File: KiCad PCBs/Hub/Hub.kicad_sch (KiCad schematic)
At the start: 1 part, among them J1 Conn_02x04_Top_Bottom

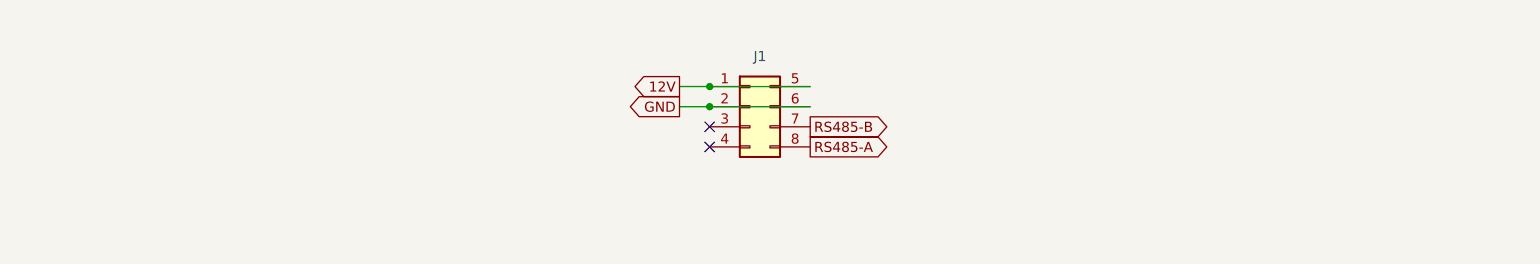
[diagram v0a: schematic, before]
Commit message: Added power status LEDs to Master PCB
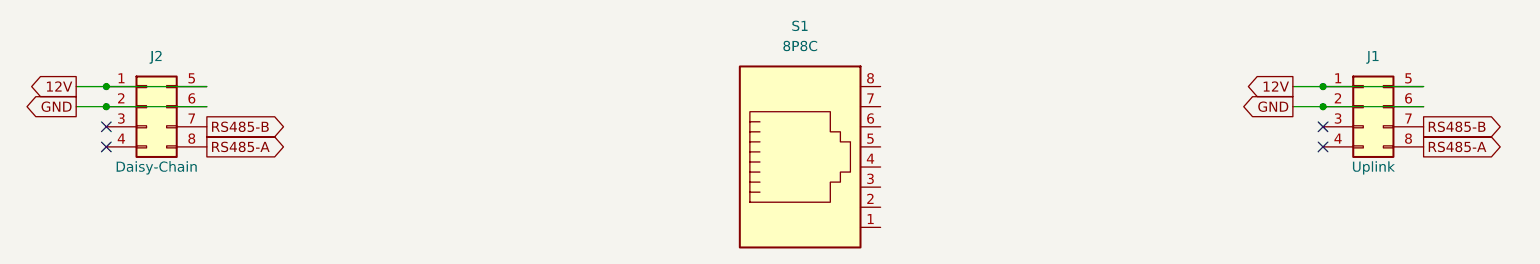
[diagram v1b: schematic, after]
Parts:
- added J2: Conn_02x04_Top_Bottom, A10 KiCad Libraries:Molex 43045-0800, symbol Connector_Generic:Conn_02x04_Top_Bottom
- added S1: 8P8C, A10 KiCad Libraries:RJ45-8P8C, symbol Connector:8P8C
- J1: Field4 (none) -> Uplink
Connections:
- net 12V: now also J2.1 (Pin_1), J2.5 (Pin_5)
- net GND: now also J2.2 (Pin_2), J2.6 (Pin_6)
- net RS485-A: now also J2.8 (Pin_8)
- net RS485-B: now also J2.7 (Pin_7)
- no-connect marks 2 -> 4
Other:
- moved on the sheet: J1
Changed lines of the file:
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@@
 (kicad_sch (version 20211123) (generator eeschema)
   (paper "A4")
-  (junction (at 138.43 104.14) (diameter 0) (color 0 0 0 0)
+  (junction (at 215.9 104.14) (diameter 0) (color 0 0 0 0)
   )
-  (junction (at 138.43 106.68) (diameter 0) (color 0 0 0 0)
+  (junction (at 62.23 104.14) (diameter 0) (color 0 0 0 0)
   )
-  (no_connect (at 138.43 109.22))
-  (no_connect (at 138.43 111.76))
-  (wire (pts (xy 138.43 104.14) (xy 151.13 104.14))
+  (junction (at 215.9 106.68) (diameter 0) (color 0 0 0 0)
+  )
+  (junction (at 62.23 106.68) (diameter 0) (color 0 0 0 0)
+  )
+  (no_connect (at 62.23 109.22))
+  (no_connect (at 215.9 109.22))
+  (no_connect (at 62.23 111.76))
+  (no_connect (at 215.9 111.76))
+  (wire (pts (xy 215.9 104.14) (xy 228.6 104.14))
     (stroke (width 0) (type default) (color 0 0 0 0))
   )
-  (wire (pts (xy 134.62 104.14) (xy 138.43 104.14))
+  (wire (pts (xy 212.09 104.14) (xy 215.9 104.14))
     (stroke (width 0) (type default) (color 0 0 0 0))
   )
-  (wire (pts (xy 138.43 106.68) (xy 151.13 106.68))
+  (wire (pts (xy 58.42 104.14) (xy 62.23 104.14))
     (stroke (width 0) (type default) (color 0 0 0 0))
   )
-  (wire (pts (xy 134.62 106.68) (xy 138.43 106.68))
+  (wire (pts (xy 62.23 106.68) (xy 74.93 106.68))
     (stroke (width 0) (type default) (color 0 0 0 0))
   )
-  (global_label "RS485-A" (shape output) (at 151.13 111.76 0) (fields_autoplaced)
+  (wire (pts (xy 215.9 106.68) (xy 228.6 106.68))
+    (stroke (width 0) (type default) (color 0 0 0 0))
+  )
+  (wire (pts (xy 62.23 104.14) (xy 74.93 104.14))
+    (stroke (width 0) (type default) (color 0 0 0 0))
+  )
+  (wire (pts (xy 58.42 106.68) (xy 62.23 106.68))
+    (stroke (width 0) (type default) (color 0 0 0 0))
+  )
+  (wire (pts (xy 212.09 106.68) (xy 215.9 106.68))
+    (stroke (width 0) (type default) (color 0 0 0 0))
+  )
+  (global_label "RS485-A" (shape output) (at 228.6 111.76 0) (fields_autoplaced)
     (effects (font (size 1.27 1.27)) (justify left))
-    (property "Intersheet References" "${INTERSHEET_REFS}" (id 0) (at 162.3121 111.6806 0)
+    (property "Intersheet References" "${INTERSHEET_REFS}" (id 0) (at 239.7821 111.6806 0)
       (effects (font (size 1.27 1.27)) (justify left) hide)
     )
   )
-  (global_label "12V" (shape output) (at 134.62 104.14 180) (fields_autoplaced)
+  (global_label "GND" (shape output) (at 58.42 106.68 180) (fields_autoplaced)
     (effects (font (size 1.27 1.27)) (justify right))
-    (property "Intersheet References" "${INTERSHEET_REFS}" (id 0) (at 128.6993 104.0606 0)
+    (property "Intersheet References" "${INTERSHEET_REFS}" (id 0) (at 52.1364 106.6006 0)
       (effects (font (size 1.27 1.27)) (justify right) hide)
     )
   )
-  (global_label "RS485-B" (shape output) (at 151.13 109.22 0) (fields_autoplaced)
+  (global_label "12V" (shape output) (at 58.42 104.14 180) (fields_autoplaced)
+    (effects (font (size 1.27 1.27)) (justify right))
+    (property "Intersheet References" "${INTERSHEET_REFS}" (id 0) (at 52.4993 104.0606 0)
+      (effects (font (size 1.27 1.27)) (justify right) hide)
+    )
+  )
+  (global_label "RS485-B" (shape output) (at 74.93 109.22 0) (fields_autoplaced)
     (effects (font (size 1.27 1.27)) (justify left))
-    (property "Intersheet References" "${INTERSHEET_REFS}" (id 0) (at 162.4936 109.1406 0)
+    (property "Intersheet References" "${INTERSHEET_REFS}" (id 0) (at 86.2936 109.1406 0)
       (effects (font (size 1.27 1.27)) (justify left) hide)
     )
   )
-  (global_label "GND" (shape output) (at 134.62 106.68 180) (fields_autoplaced)
+  (global_label "12V" (shape output) (at 212.09 104.14 180) (fields_autoplaced)
     (effects (font (size 1.27 1.27)) (justify right))
-    (property "Intersheet References" "${INTERSHEET_REFS}" (id 0) (at 128.3364 106.6006 0)
+    (property "Intersheet References" "${INTERSHEET_REFS}" (id 0) (at 206.1693 104.0606 0)
       (effects (font (size 1.27 1.27)) (justify right) hide)
     )
   )
-  (symbol (lib_id "Connector_Generic:Conn_02x04_Top_Bottom") (at 143.51 106.68 0) (unit 1)
+  (global_label "RS485-A" (shape output) (at 74.93 111.76 0) (fields_autoplaced)
+    (effects (font (size 1.27 1.27)) (justify left))
+    (property "Intersheet References" "${INTERSHEET_REFS}" (id 0) (at 86.1121 111.6806 0)
+      (effects (font (size 1.27 1.27)) (justify left) hide)
+    )
+  )
+  (global_label "RS485-B" (shape output) (at 228.6 109.22 0) (fields_autoplaced)
+    (effects (font (size 1.27 1.27)) (justify left))
+    (property "Intersheet References" "${INTERSHEET_REFS}" (id 0) (at 239.9636 109.1406 0)
+      (effects (font (size 1.27 1.27)) (justify left) hide)
+    )
+  )
+  (global_label "GND" (shape output) (at 212.09 106.68 180) (fields_autoplaced)
+    (effects (font (size 1.27 1.27)) (justify right))
+    (property "Intersheet References" "${INTERSHEET_REFS}" (id 0) (at 205.8064 106.6006 0)
+      (effects (font (size 1.27 1.27)) (justify right) hide)
+    )
+  )
+  (symbol (lib_id "Connector_Generic:Conn_02x04_Top_Bottom") (at 220.98 106.68 0) (unit 1)
     (in_bom yes) (on_board yes)
-    (property "Reference" "J1" (id 0) (at 144.78 100.33 0))
-    (property "Value" "Conn_02x04_Top_Bottom" (id 1) (at 144.78 100.33 0)
+    (property "Reference" "J1" (id 0) (at 222.25 100.33 0))
+    (property "Value" "Conn_02x04_Top_Bottom" (id 1) (at 222.25 100.33 0)
       (effects (font (size 1.27 1.27)) hide)
     )
-    (property "Footprint" "A10 KiCad Libraries:Molex 43045-0800" (id 2) (at 143.51 106.68 0)
+    (property "Footprint" "A10 KiCad Libraries:Molex 43045-0800" (id 2) (at 220.98 106.68 0)
       (effects (font (size 1.27 1.27)) hide)
     )
-    (property "Datasheet" "~" (id 3) (at 143.51 106.68 0)
+    (property "Datasheet" "~" (id 3) (at 220.98 106.68 0)
       (effects (font (size 1.27 1.27)) hide)
     )
+    (property "Field4" "Uplink" (id 4) (at 222.25 114.3 0))
+    (pin "1")
+    (pin "2")
+    (pin "3")
+    (pin "4")
+    (pin "5")
+    (pin "6")
+    (pin "7")
+    (pin "8")
+  )
+  (symbol (lib_id "Connector:8P8C") (at 149.86 114.3 0) (unit 1)
+    (in_bom yes) (on_board yes) (fields_autoplaced)
+    (property "Reference" "S1" (id 0) (at 149.86 96.52 0))
+    (property "Value" "8P8C" (id 1) (at 149.86 99.06 0))
+    (property "Footprint" "A10 KiCad Libraries:RJ45-8P8C" (id 2) (at 149.86 113.665 90)
+      (effects (font (size 1.27 1.27)) hide)
+    )
+    (property "Datasheet" "~" (id 3) (at 149.86 113.665 90)
+      (effects (font (size 1.27 1.27)) hide)
+    )
+    (pin "1")
+    (pin "2")
+    (pin "3")
+    (pin "4")
+    (pin "5")
+    (pin "6")
+    (pin "7")
+    (pin "8")
+  )
+  (symbol (lib_id "Connector_Generic:Conn_02x04_Top_Bottom") (at 67.31 106.68 0) (unit 1)
+    (in_bom yes) (on_board yes)
+    (property "Reference" "J2" (id 0) (at 68.58 100.33 0))
+    (property "Value" "Conn_02x04_Top_Bottom" (id 1) (at 68.58 100.33 0)
+      (effects (font (size 1.27 1.27)) hide)
+    )
+    (property "Footprint" "A10 KiCad Libraries:Molex 43045-0800" (id 2) (at 67.31 106.68 0)
+      (effects (font (size 1.27 1.27)) hide)
+    )
+    (property "Datasheet" "~" (id 3) (at 67.31 106.68 0)
+      (effects (font (size 1.27 1.27)) hide)
+    )
+    (property "Field4" "Daisy-Chain" (id 4) (at 68.58 114.3 0))
     (pin "1")
     (pin "2")
@@
       (reference "J1") (unit 1) (value "Conn_02x04_Top_Bottom") (footprint "A10 KiCad Libraries:Molex 43045-0800")
     )
+    (path "/f3838ace-e55c-44ba-83f3-9fab14bb9d00"
+      (reference "J2") (unit 1) (value "Conn_02x04_Top_Bottom") (footprint "A10 KiCad Libraries:Molex 43045-0800")
+    )
+    (path "/326a8d94-eb30-43b8-8aed-9cea4f3abf49"
+      (reference "S1") (unit 1) (value "8P8C") (footprint "A10 KiCad Libraries:RJ45-8P8C")
+    )
   )

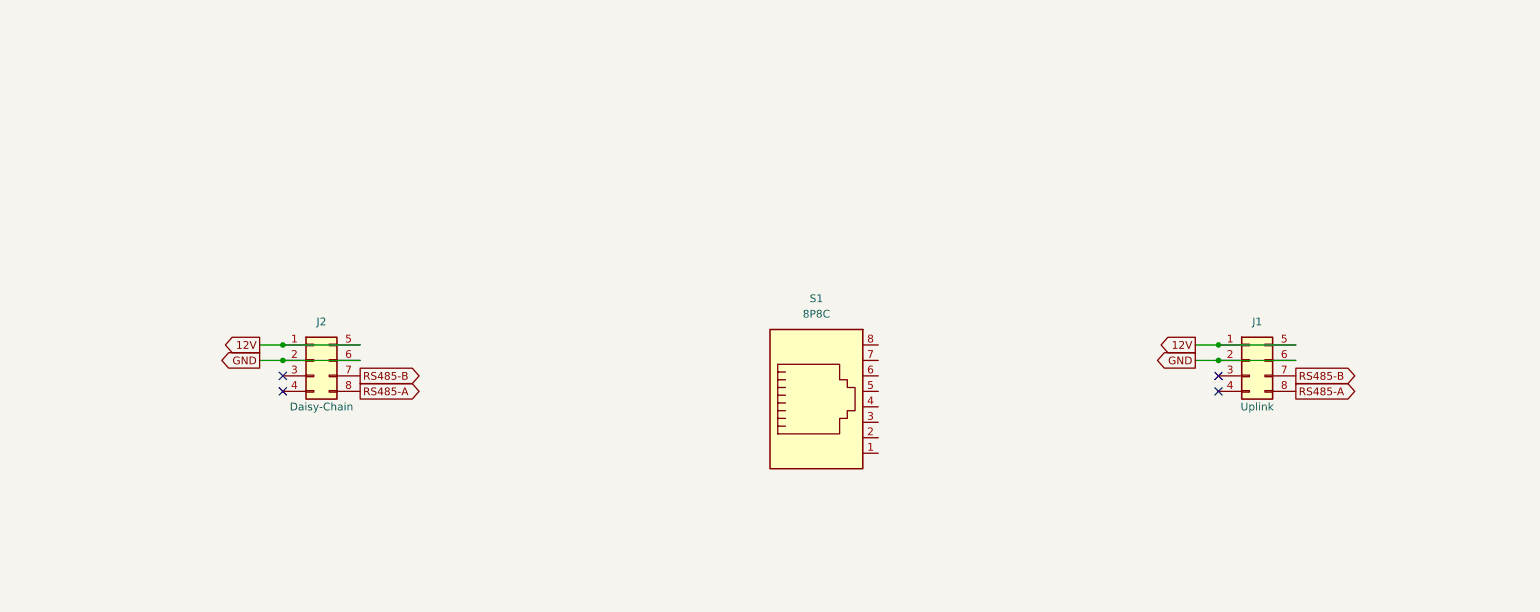
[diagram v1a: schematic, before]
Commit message: Updated Master PCB and completed first version of Hub
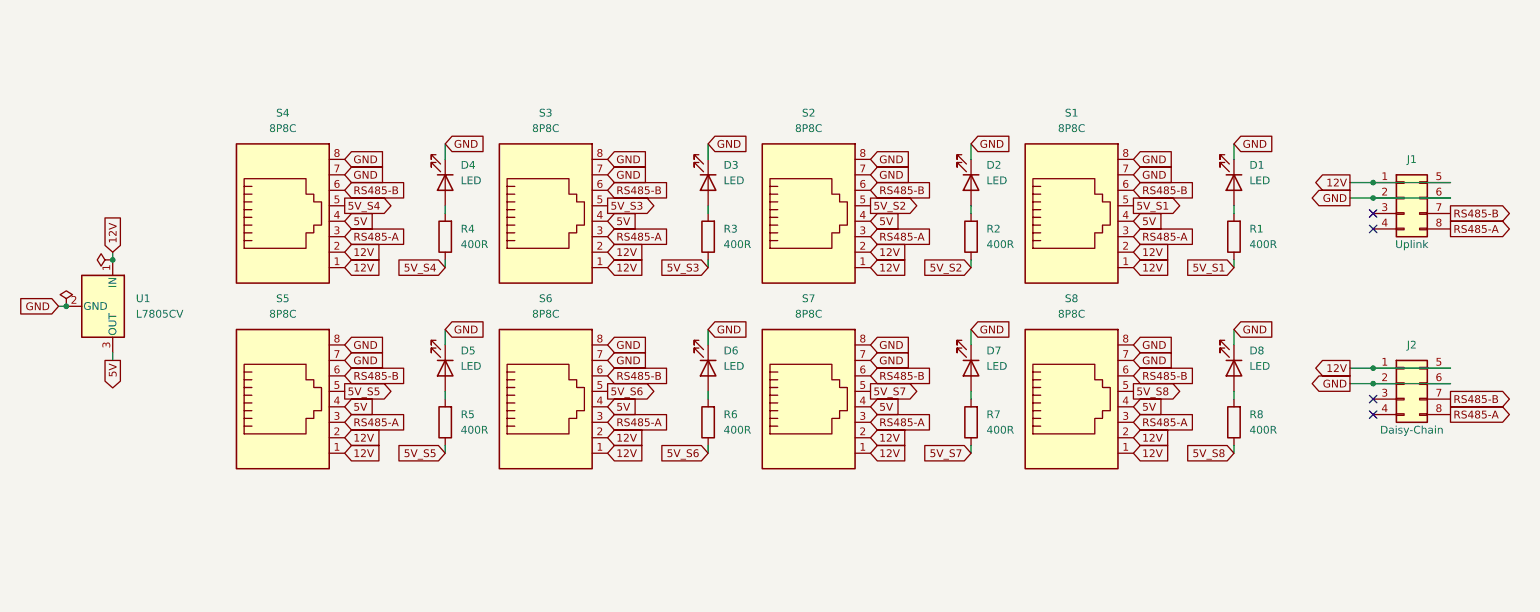
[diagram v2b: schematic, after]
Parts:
- added D1, D2, D3, D4, D5, D6, D7, D8: LED, LED_SMD:LED_1210_3225Metric_Pad1.42x2.65mm_HandSolder, symbol Device:LED
- added R1, R2, R3, R4, R5, R6, R7, R8: 400R, Resistor_SMD:R_1210_3225Metric_Pad1.30x2.65mm_HandSolder, symbol Device:R
- added S2, S3, S4, S5, S6, S7, S8: 8P8C, A10 KiCad Libraries:RJ45-8P8C, symbol Connector:8P8C
- added U1: L7805CV, Package_TO_SOT_THT:TO-220-3_Vertical, symbol Regulator_Linear:L7805
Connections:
- net 12V: now also S1.1, S1.2, S2.1, S2.2, S3.1, S3.2, S4.1, S4.2, S5.1, S5.2, S6.1, S6.2, S7.1, S7.2, S8.1, S8.2, U1.1 (IN)
- net GND: now also S1.7, S1.8, D1.1 (K), D2.1 (K), D3.1 (K), D4.1 (K), D5.1 (K), D6.1 (K), D7.1 (K), D8.1 (K), S2.7, S2.8, S3.7, S3.8, S4.7, S4.8, S5.7, S5.8, S6.7, S6.8, S7.7, S7.8, S8.7, S8.8, U1.2 (GND)
- net RS485-A: now also S1.3, S2.3, S3.3, S4.3, S5.3, S6.3, S7.3, S8.3
- net RS485-B: now also S1.6, S2.6, S3.6, S4.6, S5.6, S6.6, S7.6, S8.6
- net 5V: now reaches S1.4
- net 5V: now also S2.4, S3.4, S4.4, S5.4, S6.4, S7.4, S8.4, U1.3 (OUT)
- net 5V_S1: now reaches S1.5
- net 5V_S1: now also R1.1
- new net: D6.2 (A), R6.2
- new net: D5.2 (A), R5.2
- new net: D2.2 (A), R2.2
- new net: D4.2 (A), R4.2
- new net: D7.2 (A), R7.2
- new net: D8.2 (A), R8.2
- new net: D1.2 (A), R1.2
- new net: D3.2 (A), R3.2
- new net 5V_S2: R2.1, S2.5
- new net 5V_S3: R3.1, S3.5
- new net 5V_S4: R4.1, S4.5
- new net 5V_S5: R5.1, S5.5
- new net 5V_S6: R6.1, S6.5
- new net 5V_S7: R7.1, S7.5
- new net 5V_S8: R8.1, S8.5
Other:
- moved on the sheet: J1, J2, S1

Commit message: First version of Hub completed
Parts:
- removed D1, D2, D3, D4, D5, D6, D7, D8: LED, LED_SMD:LED_1210_3225Metric_Pad1.42x2.65mm_HandSolder, symbol Device:LED
- removed S1, S2, S3, S4, S5, S6, S7, S8: 8P8C, A10 KiCad Libraries:RJ45-8P8C, symbol Connector:8P8C
- removed U1: L7805CV, Package_TO_SOT_THT:TO-220-3_Vertical, symbol Regulator_Linear:L7805
- added R10, R12, R14, R16: 1.8K, A10 KiCad Libraries:R0805, symbol Device:R
- added R11, R13, R15, R9: 390R, A10 KiCad Libraries:R0805, symbol Device:R
- added U2, U3: RJ45-B-1*4, A10 KiCad Libraries:RJ45-TH_B-1-4, symbol A10:RJ45-B-1*4
- J1, J2: footprint A10 KiCad Libraries:Molex 43045-0800 -> A10 KiCad Libraries:Molex Micro-Fit 3.0 43045-0800
- R1, R3, R5, R7: value 400R -> 390R; footprint Resistor_SMD:R_1210_3225Metric_Pad1.30x2.65mm_HandSolder -> A10 KiCad Libraries:R0805
- R2, R4, R6, R8: value 400R -> 1.8K; footprint Resistor_SMD:R_1210_3225Metric_Pad1.30x2.65mm_HandSolder -> A10 KiCad Libraries:R0805
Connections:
- net 12V: now also U2.12, U2.16, U2.17, U2.24, U2.28, U2.29, U2.36, U2.4, U2.40, U2.41, U2.48, U2.5, U3.12, U3.16, U3.17, U3.24, U3.28, U3.29, U3.36, U3.4, U3.40, U3.41, U3.48, U3.5
- net 5V_S1: now also U2.1, U2.10; no longer R1.1
- net 5V_S2: now also U2.13, U2.22; no longer R2.1
- net 5V_S3: now also U2.25, U2.34; no longer R3.1
- net 5V_S4: now also U2.37, U2.46; no longer R4.1
- net 5V_S5: now also U3.1, U3.10; no longer R5.1
- net 5V_S6: now also U3.13, U3.22; no longer R6.1
- net 5V_S7: now also U3.25, U3.34; no longer R7.1
- net 5V_S8: now also U3.37, U3.46; no longer R8.1
- net GND: now also R1.1, R2.1, R3.1, R4.1, R5.1, R6.1, R7.1, R8.1, R10.1, R11.1, R12.1, R13.1, R14.1, R15.1, R16.1, R9.1, U2.0, U2.19, U2.20, U2.31, U2.32, U2.43, U2.44, U2.7, U2.8, U3.0, U3.19, U3.20, U3.31, U3.32, U3.43, U3.44, U3.7, U3.8
- net at R6.2: now also U2.23
- net at R5.2: now also U2.21
- net at R2.2: now also U2.11
- net at R4.2: now also U3.11
- net at R7.2: now also U3.21
- net at R8.2: now also U3.23
- net at R1.2: now also U2.9
- net at R3.2: now also U3.9
- net RS485-A renamed RS485+
- net RS485+: now also U2.15, U2.27, U2.3, U2.39, U3.15, U3.27, U3.3, U3.39
- net RS485-B renamed RS485-
- net RS485-: now also U2.18, U2.30, U2.42, U2.6, U3.18, U3.30, U3.42, U3.6
- new net: R14.2, U2.47
- new net: R13.2, U2.45
- new net: R15.2, U3.45
- new net: R9.2, U2.33
- new net: R10.2, U2.35
- new net: R11.2, U3.33
- new net: R12.2, U3.35
- new net: R16.2, U3.47

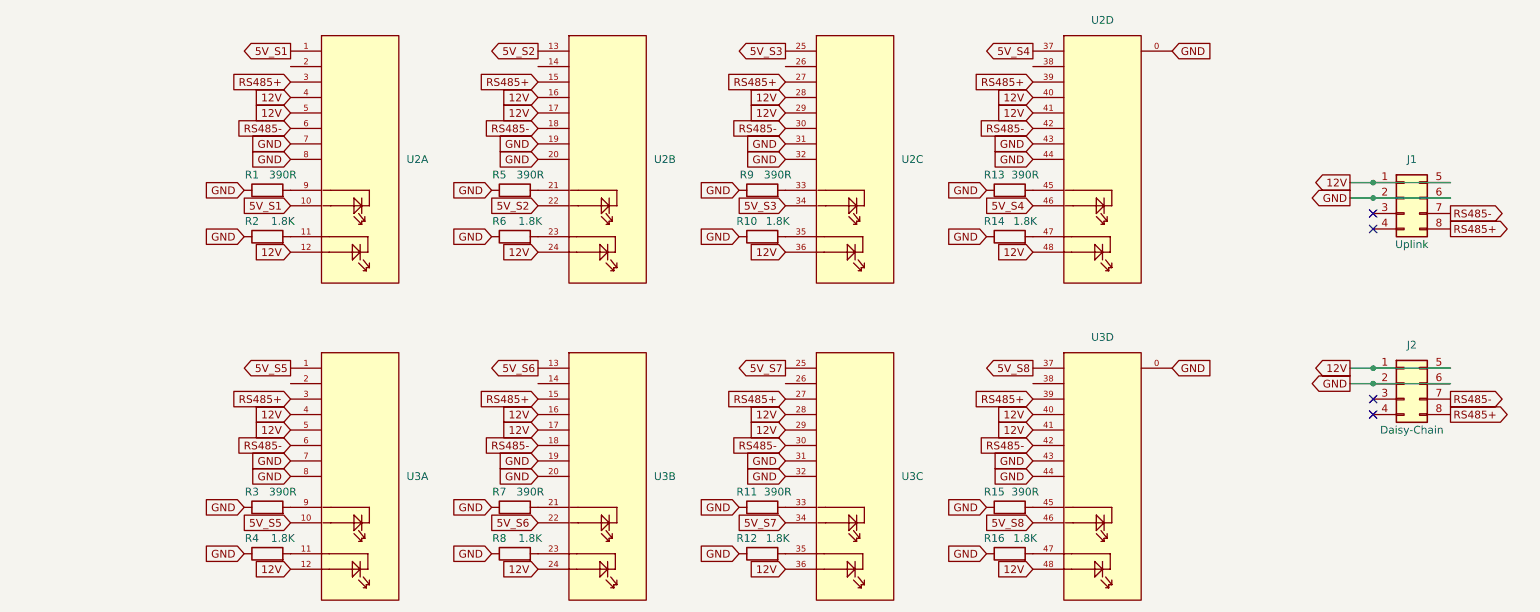
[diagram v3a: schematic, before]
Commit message: Added some more silkscreen info to Hub
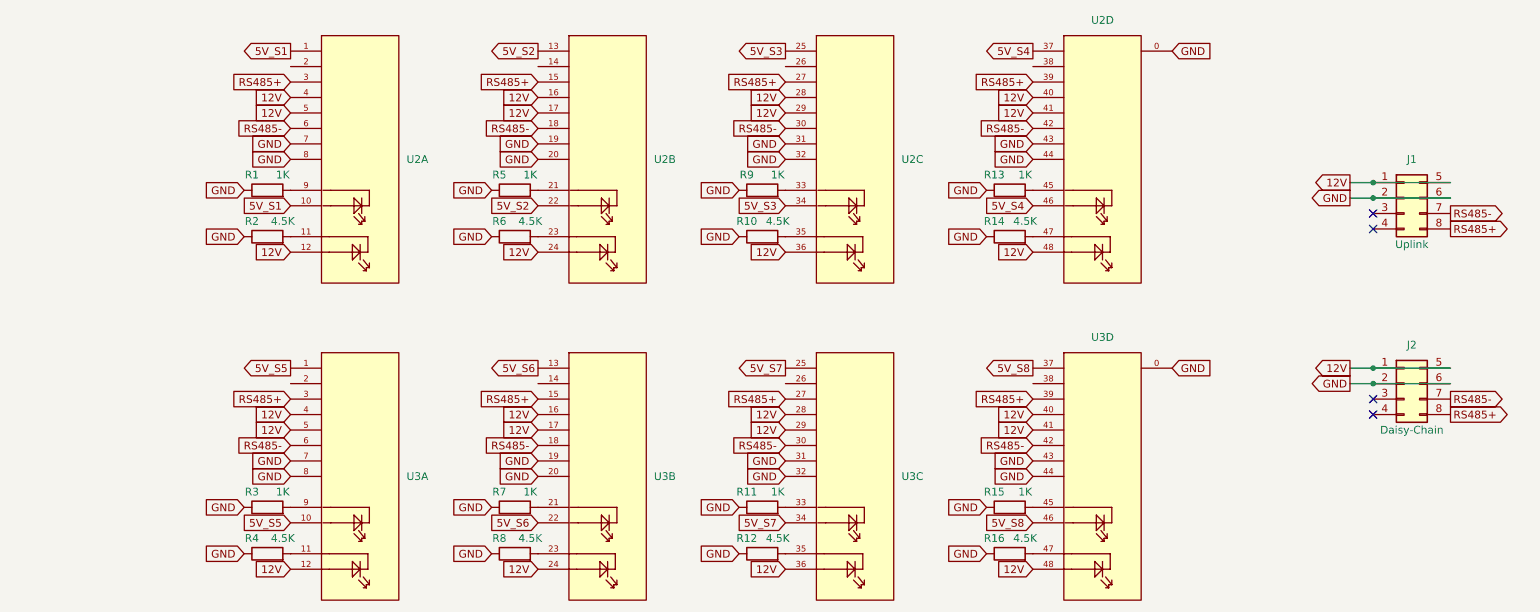
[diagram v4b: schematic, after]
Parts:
- J1, J2: LCSC (none) -> C234189; now left out of the parts list
- R1, R11, R13, R15, R3, R5, R7, R9: value 390R -> 1K; LCSC (none) -> C17513
- R10, R12, R14, R16, R2, R4, R6, R8: value 1.8K -> 4.5K; LCSC (none) -> C17673

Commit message: Updated HUB LEDs
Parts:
- added D1: BLUE, LED_SMD:LED_0603_1608Metric, symbol Device:LED
- added R17: 1.8K, A10 KiCad Libraries:R0805, symbol Device:R
- R10, R12, R14, R16, R2, R4, R6, R8: value 4.5K -> 1K; LCSC C17673 -> C17513
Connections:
- net 12V: now also R17.1; no longer U2.12, U2.24, U2.36, U2.48, U3.12, U3.24, U3.36, U3.48
- net GND: now also D1.1 (K)
- net ACT1: now reaches U2.2
- net ACT1: now also U2.12
- net ACT2: now reaches U2.14
- net ACT2: now also U2.24
- net ACT7: now reaches U3.26
- net ACT7: now also U3.36
- net ACT5: now reaches U3.2
- net ACT5: now also U3.12
- net ACT4: now reaches U2.38
- net ACT4: now also U2.48
- net ACT8: now reaches U3.38
- net ACT8: now also U3.48
- net ACT6: now reaches U3.14
- net ACT6: now also U3.24
- net ACT3: now reaches U2.26
- net ACT3: now also U2.36
- net 5V_S1 renamed PLED1
- net 5V_S2 renamed PLED2
- net 5V_S3 renamed PLED3
- net 5V_S4 renamed PLED4
- net 5V_S5 renamed PLED5
- net 5V_S6 renamed PLED6
- net 5V_S7 renamed PLED7
- net 5V_S8 renamed PLED8
- new net: D1.2 (A), R17.2
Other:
- moved on the sheet: J2
